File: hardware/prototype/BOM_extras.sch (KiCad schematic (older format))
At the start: 14 parts, among them J10 Conn_02x12_Odd_Even, J11 Conn_02x12_Odd_Even, J12 Conn_01x02, J13 Conn_02x07_Odd_Even, J14 Conn_02x07_Odd_Even, J15 Conn_01x08, J16 Conn_01x08, J17 RJ45, J18 RJ45_LEDS, J19 Conn_01x04, J20 RJ45-TRANSFO, J8 Conn_01x19, J9 Conn_01x19

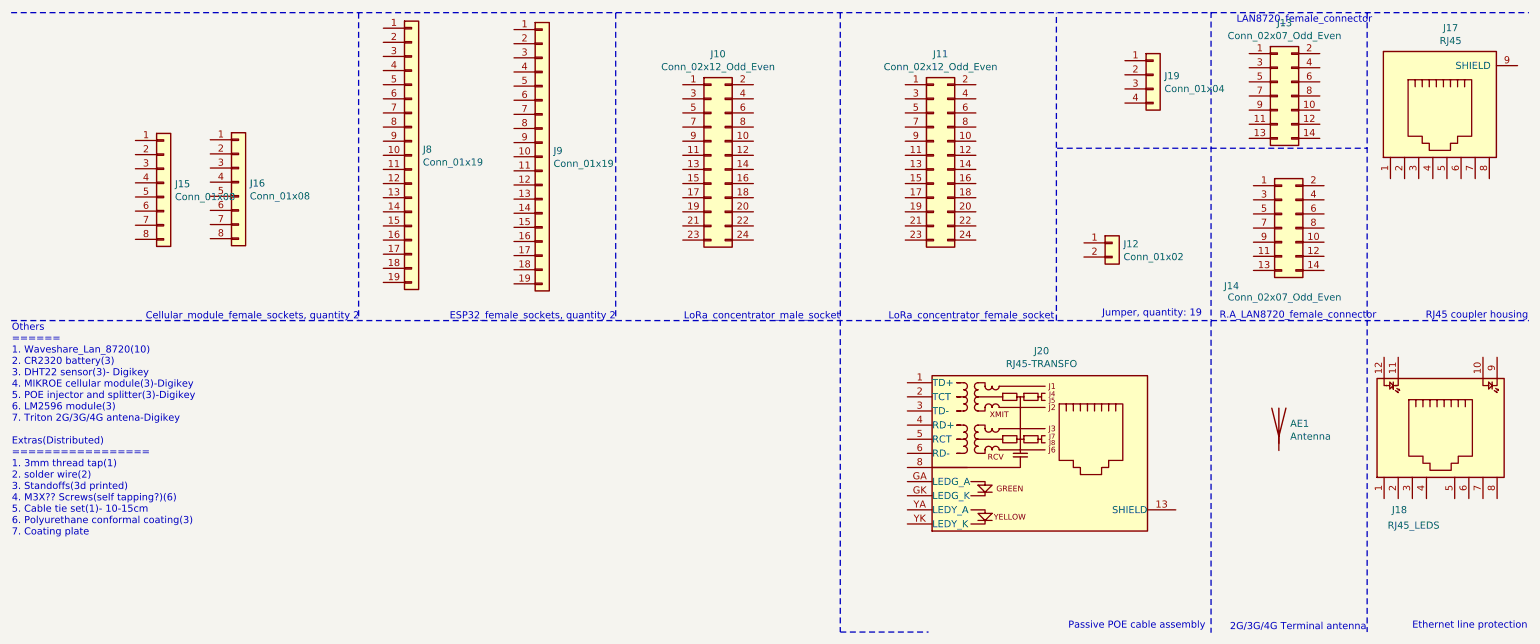
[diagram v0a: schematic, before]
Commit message: Add main file
1. Update README
2. Add BOM
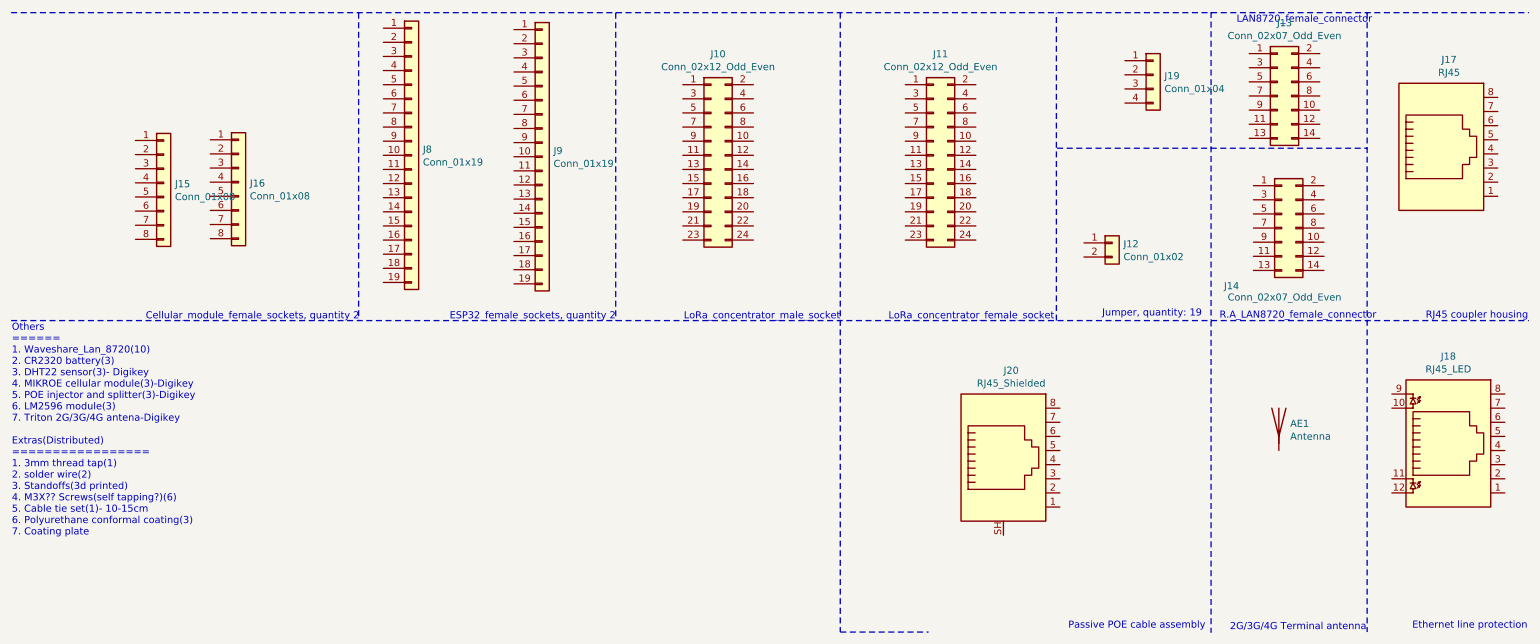
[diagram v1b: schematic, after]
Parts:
- removed J17: RJ45, symbol Connector_Specialized:RJ45
- removed J18: RJ45_LEDS, symbol Connector_Specialized:RJ45_LEDS
- removed J20: RJ45-TRANSFO, symbol Connector_Specialized:RJ45-TRANSFO
- added J17: RJ45, symbol Connector:RJ45
- added J18: RJ45_LED, symbol Connector:RJ45_LED
- added J20: RJ45_Shielded, symbol Connector:RJ45_Shielded
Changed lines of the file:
@@
-	1    0    0    -1
-$EndComp
-$Comp
-L Connector_Specialized:RJ45 J17
-U 1 1 5AEC9070
-P 10590 2875
-F 0 "J17" H 10666 3492 50  0000 C CNN
-F 1 "RJ45" H 10666 3401 50  0000 C CNN
-F 2 "" H 10590 2875 50  0001 C CNN
-F 3 "" H 10590 2875 50  0001 C CNN
-F 4 "RCP-5SPFFH-TCU7001 " H 10590 2875 50  0001 C CNN "manf#"
-	1    10590 2875
 	1    0    0    -1
 $EndComp
 Text Notes 11215 4325 2    50   ~ 0
 RJ45 coupler housing
-$Comp
-L Connector_Specialized:RJ45_LEDS J18
-U 1 1 5AED1D78
-P 10595 5090
-F 0 "J18" H 10250 4510 50  0000 L CNN
-F 1 "RJ45_LEDS" H 10220 4400 50  0000 L CNN
-F 2 "" H 10595 5040 50  0001 C CNN
-F 3 "" H 10595 5040 50  0001 C CNN
-F 4 "ESP-100-POE " H 10595 5090 50  0001 C CNN "manf#"
-	1    10595 5090
-	1    0    0    -1
-$EndComp
 Wire Notes Line
 	10075 2150 10075 6535
@@
 Text Notes 10070 6530 2    50   ~ 0
 2G/3G/4G Terminal antenna
-$Comp
-L Connector_Specialized:RJ45-TRANSFO J20
-U 1 1 5AEFB180
-P 8120 5270
-F 0 "J20" H 7770 5995 50  0000 C CNN
-F 1 "RJ45-TRANSFO" H 7770 5904 50  0000 C CNN
-F 2 "" H 8120 5770 50  0001 C CNN
-F 3 "~" H 8220 5870 50  0001 C CNN
-F 4 "1528-1773-ND " H 8120 5270 50  0001 C CNN "manf#"
-	1    8120 5270
-	1    0    0    -1
-$EndComp
 Wire Notes Line
 	6345 6535 6970 6535
@@
 Text Notes 8930 6520 2    50   ~ 0
 Passive POE cable assembly
+$Comp
+L Connector:RJ45 J17
+U 1 1 5AF97458
+P 10600 3150
+F 0 "J17" H 10655 3817 50  0000 C CNN
+F 1 "RJ45" H 10655 3726 50  0000 C CNN
+F 2 "" V 10600 3175 50  0001 C CNN
+F 3 "~" V 10600 3175 50  0001 C CNN
+F 4 "RCP-5SPFFH-TCU7001 " H 10600 3150 50  0001 C CNN "manf#"
+	1    10600 3150
+	1    0    0    -1
+$EndComp
+$Comp
+L Connector:RJ45_LED J18
+U 1 1 5AF9804C
+P 10650 5250
+F 0 "J18" H 10650 5917 50  0000 C CNN
+F 1 "RJ45_LED" H 10650 5826 50  0000 C CNN
+F 2 "" V 10650 5275 50  0001 C CNN
+F 3 "" V 10650 5275 50  0001 C CNN
+F 4 "ESP-100-POE " H 10650 5250 50  0001 C CNN "manf#"
+	1    10650 5250
+	1    0    0    -1
+$EndComp
+$Comp
+L Connector:RJ45_Shielded J20
+U 1 1 5AF986FC
+P 7500 5350
+F 0 "J20" H 7555 6017 50  0000 C CNN
+F 1 "RJ45_Shielded" H 7555 5926 50  0000 C CNN
+F 2 "" V 7500 5375 50  0001 C CNN
+F 3 "~" V 7500 5375 50  0001 C CNN
+F 4 "1528-1773-ND " H 7500 5350 50  0001 C CNN "manf#"
+	1    7500 5350
+	1    0    0    -1
+$EndComp
 $EndSCHEMATC
